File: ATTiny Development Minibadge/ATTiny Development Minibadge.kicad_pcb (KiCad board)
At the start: 2 copper layers, 20.4 x 20.5 mm, 17 parts, among them J1 SPI, J2 I2C, J3 DAC, J4 USART, U1 ATtiny816-M

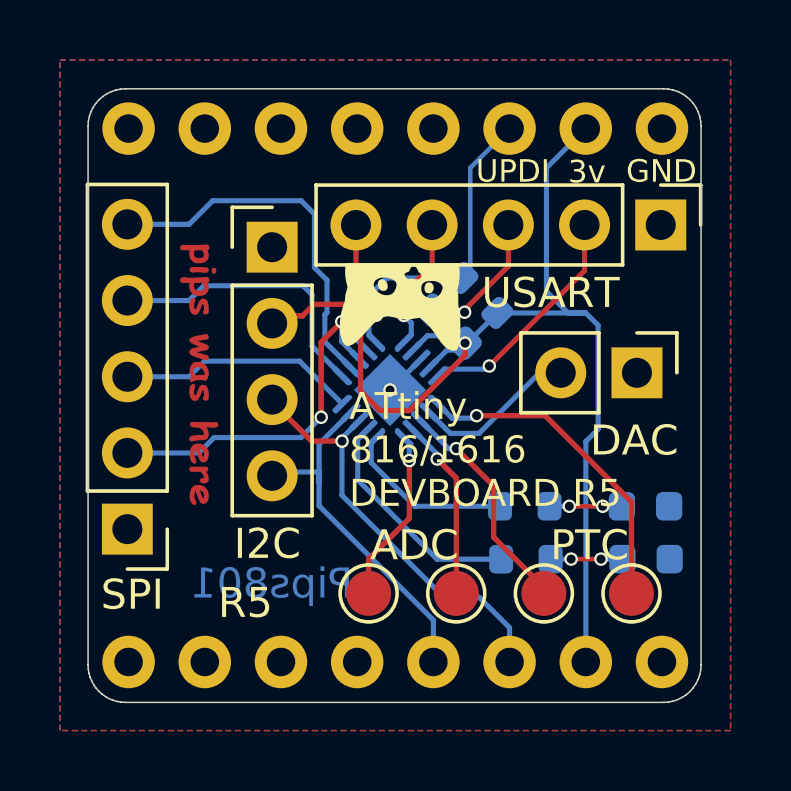
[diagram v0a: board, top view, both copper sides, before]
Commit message: R6
Add diode for reverse polarity protection
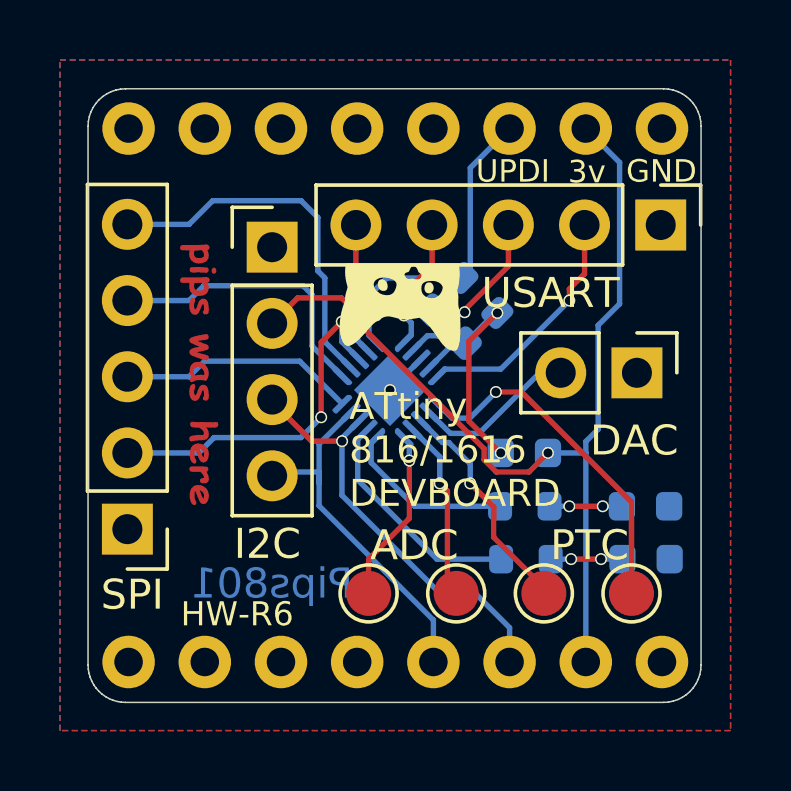
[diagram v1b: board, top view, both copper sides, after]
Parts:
- added D3: 20V, Diode_SMD:D_0603_1608Metric, B.Cu at (108.1, 67.6)
- U1: value ATtiny816-M -> ATtiny816/1616-M
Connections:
- C1 pad 2: +3.3V -> Net-(D3-K)
- R3 pad 1: +3.3V -> Net-(D3-K)
- U1 pad 4: +3.3V -> Net-(D3-K)
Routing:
- net Net-(D3-K): track 0.00 -> 8.56 mm, vias 0 -> 2
- net +3.3V: track 36.7 -> 32.7 mm
- net PTC_X1/Y1: track 10.7 -> 11.3 mm
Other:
- board text added: "ATtiny 816/1616 DEVBOARD"
- board text added: "HW-${REVISION}"
- board text removed: "${REVISION}"
- board text removed: "ATtiny 816/1616 DEVBOARD ${REVISION}"
